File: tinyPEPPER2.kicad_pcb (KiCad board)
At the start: 2 copper layers, 20 x 22.6 mm, 91 parts, among them U201 EFM8BB10, U301 EFM8BB10, U401 EFM8BB10, U501 EFM8BB10

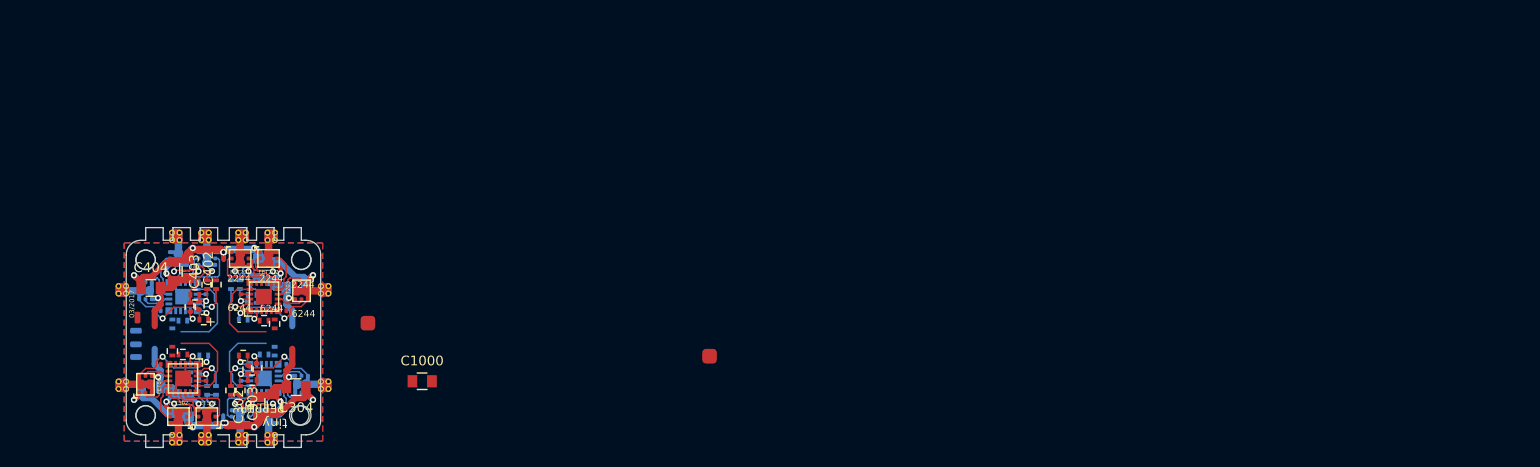
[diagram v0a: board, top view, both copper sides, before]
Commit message: adding gate druiver
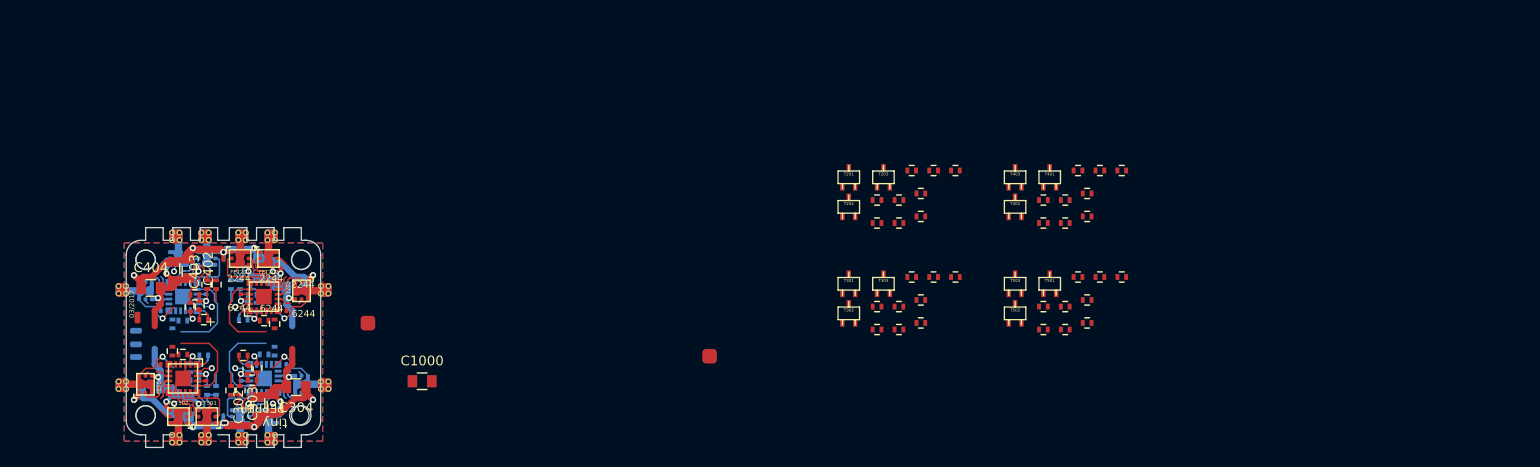
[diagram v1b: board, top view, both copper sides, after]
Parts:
- added R208: 2k2, custom:R_0402_CUSTOM, F.Cu at (180.8, 92.8)
- added R209: 2k2, custom:R_0402_CUSTOM, F.Cu at (177.2, 95.9)
- added R210: 2k2, custom:R_0402_CUSTOM, F.Cu at (181.7, 95.2)
- added R211: 1K, custom:R_0402_CUSTOM, F.Cu at (179.5, 98.2)
- added R212: 1K, custom:R_0402_CUSTOM, F.Cu at (185.3, 92.8)
- added R213: 1K, custom:R_0402_CUSTOM, F.Cu at (183.0, 92.8)
- added R217: 10k, custom:R_0402_CUSTOM, F.Cu at (181.7, 97.5)
- added R218: 10k, custom:R_0402_CUSTOM, F.Cu at (179.5, 95.9)
- added R219: 10k, custom:R_0402_CUSTOM, F.Cu at (177.2, 98.2)
- added R308: 2k2, custom:R_0402_CUSTOM, F.Cu at (181.7, 108.5)
- added R309: 2k2, custom:R_0402_CUSTOM, F.Cu at (185.3, 103.8)
- added R310: 2k2, custom:R_0402_CUSTOM, F.Cu at (179.5, 109.2)
- added R311: 1K, custom:R_0402_CUSTOM, F.Cu at (181.7, 106.1)
- added R312: 1K, custom:R_0402_CUSTOM, F.Cu at (183.0, 103.8)
- added R313: 1K, custom:R_0402_CUSTOM, F.Cu at (179.5, 106.8)
- added R317: 10k, custom:R_0402_CUSTOM, F.Cu at (177.2, 109.2)
- added R318: 10k, custom:R_0402_CUSTOM, F.Cu at (180.8, 103.8)
- added R319: 10k, custom:R_0402_CUSTOM, F.Cu at (177.2, 106.8)
- added R408: 2k2, custom:R_0402_CUSTOM, F.Cu at (197.9, 92.8)
- added R409: 2k2, custom:R_0402_CUSTOM, F.Cu at (194.3, 98.2)
- added R410: 2k2, custom:R_0402_CUSTOM, F.Cu at (196.6, 95.9)
- added R411: 1K, custom:R_0402_CUSTOM, F.Cu at (200.1, 92.8)
- added R412: 1K, custom:R_0402_CUSTOM, F.Cu at (198.8, 95.2)
- added R413: 1K, custom:R_0402_CUSTOM, F.Cu at (198.8, 97.5)
- added R417: 10k, custom:R_0402_CUSTOM, F.Cu at (194.3, 95.9)
- added R418: 10k, custom:R_0402_CUSTOM, F.Cu at (202.4, 92.8)
- added R419: 10k, custom:R_0402_CUSTOM, F.Cu at (196.6, 98.2)
- added R508: 2k2, custom:R_0402_CUSTOM, F.Cu at (197.9, 103.8)
- added R509: 2k2, custom:R_0402_CUSTOM, F.Cu at (194.3, 106.8)
- added R510: 2k2, custom:R_0402_CUSTOM, F.Cu at (198.8, 108.5)
- added R511: 1K, custom:R_0402_CUSTOM, F.Cu at (202.4, 103.8)
- added R512: 1K, custom:R_0402_CUSTOM, F.Cu at (196.6, 109.2)
- added R513: 1K, custom:R_0402_CUSTOM, F.Cu at (198.8, 106.1)
- added R517: 10k, custom:R_0402_CUSTOM, F.Cu at (200.1, 103.8)
- added R518: 10k, custom:R_0402_CUSTOM, F.Cu at (196.6, 106.8)
- added R519: 10k, custom:R_0402_CUSTOM, F.Cu at (194.3, 109.2)
- added T201: MMBTA06WT1G, custom:SC70, F.Cu at (174.3, 93.5)
- added T202: MMBTA06WT1G, custom:SC70, F.Cu at (174.3, 96.6)
- added T203: MMBTA06WT1G, custom:SC70, F.Cu at (177.9, 93.5)
- added T301: MMBTA06WT1G, custom:SC70, F.Cu at (174.3, 104.5)
- added T302: MMBTA06WT1G, custom:SC70, F.Cu at (174.3, 107.5)
- added T303: MMBTA06WT1G, custom:SC70, F.Cu at (177.9, 104.5)
- added T401: MMBTA06WT1G, custom:SC70, F.Cu at (195.0, 93.5)
- added T402: MMBTA06WT1G, custom:SC70, F.Cu at (191.4, 96.6)
- added T403: MMBTA06WT1G, custom:SC70, F.Cu at (191.4, 93.5)
- added T501: MMBTA06WT1G, custom:SC70, F.Cu at (195.0, 104.5)
- added T502: MMBTA06WT1G, custom:SC70, F.Cu at (191.4, 107.5)
- added T503: MMBTA06WT1G, custom:SC70, F.Cu at (191.4, 104.5)
- R202, R204, R206, R302, R304, R306, R402, R404, R406, R502, R504, R506: value 1k -> 10k
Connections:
- FET201 pad 5: /single esc 1/Ac_0 -> Net-(FET201-Pad5)
- FET202 pad 5: /single esc 1/Bc_0 -> Net-(FET202-Pad5)
- FET203 pad 5: /single esc 1/Cc_0 -> Net-(FET203-Pad5)
- FET301 pad 5: /single esc 2/Ac_0 -> Net-(FET301-Pad5)
- FET302 pad 5: /single esc 2/Bc_0 -> Net-(FET302-Pad5)
- FET303 pad 5: /single esc 2/Cc_0 -> Net-(FET303-Pad5)
- FET401 pad 5: /single esc 3/Ac_0 -> Net-(FET401-Pad5)
- FET402 pad 5: /single esc 3/Bc_0 -> Net-(FET402-Pad5)
- FET403 pad 5: /single esc 3/Cc_0 -> Net-(FET403-Pad5)
- FET501 pad 5: /single esc 4/Ac_0 -> Net-(FET501-Pad5)
- FET502 pad 5: /single esc 4/Bc_0 -> Net-(FET502-Pad5)
- FET503 pad 5: /single esc 4/Cc_0 -> Net-(FET503-Pad5)
- R201 pad 1: Net-(R201-Pad1) -> VCC
- R201 pad 2: VCC -> /single esc 1/C2CK_0
- R202 pad 2: /single esc 1/PHASE_A_0 -> Net-(R202-Pad2)
- R203 pad 1: /single esc 1/PHASE_A_0 -> Net-(R202-Pad2)
- R203 pad 2: Net-(R203-Pad2) -> /single esc 1/PHASE_A_0
- R204 pad 2: /single esc 1/PHASE_B_0 -> Net-(R204-Pad2)
- R205 pad 1: /single esc 1/PHASE_B_0 -> Net-(R204-Pad2)
- R205 pad 2: Net-(R205-Pad2) -> /single esc 1/PHASE_B_0
- R206 pad 2: /single esc 1/PHASE_C_0 -> Net-(R206-Pad2)
- R207 pad 1: /single esc 1/PHASE_C_0 -> Net-(R206-Pad2)
- R207 pad 2: Net-(R207-Pad2) -> /single esc 1/PHASE_C_0
- R301 pad 1: Net-(R301-Pad1) -> VCC
- R301 pad 2: VCC -> /single esc 2/C2CK_0
- R302 pad 2: /single esc 2/PHASE_A_0 -> Net-(R302-Pad2)
- R303 pad 1: /single esc 2/PHASE_A_0 -> Net-(R302-Pad2)
- R303 pad 2: Net-(R303-Pad2) -> /single esc 2/PHASE_A_0
- R304 pad 2: /single esc 2/PHASE_B_0 -> Net-(R304-Pad2)
- R305 pad 1: /single esc 2/PHASE_B_0 -> Net-(R304-Pad2)
- R305 pad 2: Net-(R305-Pad2) -> /single esc 2/PHASE_B_0
- R306 pad 2: /single esc 2/PHASE_C_0 -> Net-(R306-Pad2)
- R307 pad 1: /single esc 2/PHASE_C_0 -> Net-(R306-Pad2)
- R307 pad 2: Net-(R307-Pad2) -> /single esc 2/PHASE_C_0
- R401 pad 1: Net-(R401-Pad1) -> VCC
- R401 pad 2: VCC -> /single esc 3/C2CK_0
- R402 pad 2: /single esc 3/PHASE_A_0 -> Net-(R402-Pad2)
- R403 pad 1: /single esc 3/PHASE_A_0 -> Net-(R402-Pad2)
- R403 pad 2: Net-(R403-Pad2) -> /single esc 3/PHASE_A_0
- R404 pad 2: /single esc 3/PHASE_B_0 -> Net-(R404-Pad2)
- R405 pad 1: /single esc 3/PHASE_B_0 -> Net-(R404-Pad2)
- R405 pad 2: Net-(R405-Pad2) -> /single esc 3/PHASE_B_0
- R406 pad 2: /single esc 3/PHASE_C_0 -> Net-(R406-Pad2)
- R407 pad 1: /single esc 3/PHASE_C_0 -> Net-(R406-Pad2)
- R407 pad 2: Net-(R407-Pad2) -> /single esc 3/PHASE_C_0
- R501 pad 1: Net-(R501-Pad1) -> VCC
- R501 pad 2: VCC -> /single esc 4/C2CK_0
- R502 pad 2: /single esc 4/PHASE_A_0 -> Net-(R502-Pad2)
- R503 pad 1: /single esc 4/PHASE_A_0 -> Net-(R502-Pad2)
- R503 pad 2: Net-(R503-Pad2) -> /single esc 4/PHASE_A_0
- R504 pad 2: /single esc 4/PHASE_B_0 -> Net-(R504-Pad2)
- R505 pad 1: /single esc 4/PHASE_B_0 -> Net-(R504-Pad2)
- R505 pad 2: Net-(R505-Pad2) -> /single esc 4/PHASE_B_0
- R506 pad 2: /single esc 4/PHASE_C_0 -> Net-(R506-Pad2)
- R507 pad 1: /single esc 4/PHASE_C_0 -> Net-(R506-Pad2)
- R507 pad 2: Net-(R507-Pad2) -> /single esc 4/PHASE_C_0
- U201 pad 1: Net-(R207-Pad2) -> Net-(R206-Pad2)
- U201 pad 2: Net-(R205-Pad2) -> Net-(R204-Pad2)
- U201 pad 20: Net-(R203-Pad2) -> Net-(R202-Pad2)
- U201 pad 5: Net-(R201-Pad1) -> /single esc 1/C2CK_0
- U201 pad 8: /single esc 1/Cc_0 -> Net-(R213-Pad2)
- U301 pad 1: Net-(R307-Pad2) -> Net-(R306-Pad2)
- U301 pad 2: Net-(R305-Pad2) -> Net-(R304-Pad2)
- U301 pad 20: Net-(R303-Pad2) -> Net-(R302-Pad2)
- U301 pad 5: Net-(R301-Pad1) -> /single esc 2/C2CK_0
- U301 pad 8: /single esc 2/Cc_0 -> Net-(R313-Pad2)
- U401 pad 1: Net-(R407-Pad2) -> Net-(R406-Pad2)
- U401 pad 2: Net-(R405-Pad2) -> Net-(R404-Pad2)
- U401 pad 20: Net-(R403-Pad2) -> Net-(R402-Pad2)
- U401 pad 5: Net-(R401-Pad1) -> /single esc 3/C2CK_0
- U401 pad 8: /single esc 3/Cc_0 -> Net-(R413-Pad2)
- U501 pad 1: Net-(R507-Pad2) -> Net-(R506-Pad2)
- U501 pad 2: Net-(R505-Pad2) -> Net-(R504-Pad2)
- U501 pad 20: Net-(R503-Pad2) -> Net-(R502-Pad2)
- U501 pad 5: Net-(R501-Pad1) -> /single esc 4/C2CK_0
- U501 pad 8: /single esc 4/Cc_0 -> Net-(R513-Pad2)
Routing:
- net /single esc 3/PHASE_B_0: track 13.9 -> 6.85 mm
- net /single esc 1/PHASE_B_0: track 13.9 -> 6.85 mm
- net /single esc 4/PHASE_B_0: track 13.9 -> 6.85 mm
- net /single esc 2/PHASE_B_0: track 13.9 -> 6.85 mm
- net Net-(R404-Pad2): track 0.00 -> 6.74 mm, vias 0 -> 1
- net Net-(R204-Pad2): track 0.00 -> 6.74 mm, vias 0 -> 1
- net Net-(R504-Pad2): track 0.00 -> 6.74 mm, vias 0 -> 1
- net Net-(R304-Pad2): track 0.00 -> 6.74 mm, vias 0 -> 1
- net Net-(R302-Pad2): track 0.00 -> 4.07 mm, vias 0 -> 1
- net Net-(R402-Pad2): track 0.00 -> 4.07 mm, vias 0 -> 1
- net Net-(R502-Pad2): track 0.00 -> 3.78 mm, vias 0 -> 1
- net Net-(R202-Pad2): track 0.00 -> 3.78 mm, vias 0 -> 1
- net Net-(R503-Pad2): track 3.65 -> 0.00 mm, vias 1 -> 0
- net Net-(R303-Pad2): track 3.65 -> 0.00 mm, vias 1 -> 0
- net Net-(R403-Pad2): track 3.65 -> 0.00 mm, vias 1 -> 0
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
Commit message: routing test done
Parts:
- added C1001: 100n, custom:C_0402_CUSTOM, F.Cu at (89.7, 109.5)
- added C1002: 100n, custom:C_0402_CUSTOM, F.Cu at (89.7, 111.9)
- added C1003: 10n, custom:C_0402_CUSTOM, F.Cu at (105.3, 110.1)
- added R214: 100, custom:R_0603_CUSTOM, F.Cu at (215.6, 94.8)
- added R215: 100, custom:R_0603_CUSTOM, F.Cu at (220.0, 94.8)
- added R216: 100, custom:R_0603_CUSTOM, F.Cu at (224.3, 94.8)
- added R314: 100, custom:R_0603_CUSTOM, F.Cu at (215.6, 105.6)
- added R315: 100, custom:R_0603_CUSTOM, F.Cu at (220.0, 105.6)
- added R316: 100, custom:R_0603_CUSTOM, F.Cu at (224.3, 105.6)
- added R414: 100, custom:R_0603_CUSTOM, F.Cu at (232.5, 94.8)
- added R415: 100, custom:R_0603_CUSTOM, F.Cu at (236.8, 94.8)
- added R416: 100, custom:R_0603_CUSTOM, F.Cu at (241.1, 94.8)
- added R514: 100, custom:R_0603_CUSTOM, B.Cu at (109.4, 116.5)
- added R515: 100, custom:R_0603_CUSTOM, B.Cu at (105.6, 116.2)
- added R516: 100, custom:R_0603_CUSTOM, F.Cu at (102.1, 112.9)
- added U1: AP131-30, TO_SOT_Packages_SMD:SOT-23-5, F.Cu at (102.6, 110.0)
- R508, R509, R510, R511, R513, R517, R518, R519: moved to B.Cu
- T201, T202, T203, T301, T302, T303, T401, T402, T403: value MMBTA06WT1G -> BC847BTT1G; footprint custom:SC70 -> custom:SC75
- T501, T502, T503: value MMBTA06WT1G -> BC847BTT1G; footprint custom:SC70 -> custom:SC75; moved to B.Cu
- TP104, TP106: moved to F.Cu
- moved R513 95.9 mm to (103.1, 112.8)
- moved R511 95.8 mm to (107.5, 117.3), turned to 90 degrees
- moved R517 93.7 mm to (107.7, 118.8), turned to 90 degrees
- moved R519 92.9 mm to (101.5, 113.3)
- moved R510 92.8 mm to (106.2, 112.8), turned to 180 degrees
- moved R512 92.4 mm to (104.5, 116.8), turned to 180 degrees
- moved R518 91.2 mm to (105.9, 117.1), turned to 180 degrees
- moved R508 90.7 mm to (107.7, 112.8)
- moved T503 90.5 mm to (101.5, 114.9), turned to 270 degrees
- moved R509 88.3 mm to (106.3, 113.8), turned to 180 degrees
- moved T501 87.0 mm to (109.1, 118.6)
- moved T502 86.9 mm to (105.2, 118.6)
- moved C201 65.8 mm to (176.3, 86.7)
- moved C203 65.8 mm to (177.3, 81.6)
- moved OUT_A401 65.8 mm to (170.2, 78.0)
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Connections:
- C201 pad 2: VCC -> /single esc 1/3V3
- C301 pad 2: VCC -> /single esc 1/3V3
- C401 pad 2: VCC -> /single esc 1/3V3
- C501 pad 2: VCC -> /single esc 1/3V3
- R201 pad 1: VCC -> /single esc 1/3V3
- R301 pad 1: VCC -> /single esc 1/3V3
- R401 pad 1: VCC -> /single esc 1/3V3
- R501 pad 1: VCC -> /single esc 1/3V3
- T201 pad 3: (no net) -> GND
- T202 pad 3: (no net) -> GND
- T203 pad 3: (no net) -> GND
- T301 pad 3: (no net) -> GND
- T302 pad 3: (no net) -> GND
- T303 pad 3: (no net) -> GND
- T401 pad 3: (no net) -> GND
- T402 pad 3: (no net) -> GND
- T403 pad 3: (no net) -> GND
- T501 pad 3: (no net) -> GND
- T502 pad 3: (no net) -> GND
- T503 pad 3: (no net) -> GND
- U201 pad 4: VCC -> /single esc 1/3V3
- U301 pad 4: VCC -> /single esc 1/3V3
- U401 pad 4: VCC -> /single esc 1/3V3
- U501 pad 4: VCC -> /single esc 1/3V3
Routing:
- net GND: track 85.5 -> 44.5 mm, vias 12 -> 5
- net VCC: track 59.6 -> 33.9 mm, vias 12 -> 4
- net (no net): track 0.00 -> 17.7 mm
- net /single esc 3/PHASE_C_0: track 10.9 -> 0.00 mm, vias 1 -> 0
- net /single esc 1/PHASE_C_0: track 10.9 -> 0.00 mm, vias 1 -> 0
- net /single esc 2/PHASE_C_0: track 10.9 -> 0.00 mm, vias 1 -> 0
- net /single esc 3/RC_IN: track 9.27 -> 0.00 mm
- net /RC_IN_0: track 9.27 -> 0.00 mm
- net /RC_IN_1: track 9.27 -> 0.00 mm
- net /single esc 2/PHASE_A_0: track 7.72 -> 0.00 mm
- net /single esc 1/PHASE_A_0: track 7.72 -> 0.00 mm
- net /single esc 3/PHASE_A_0: track 7.72 -> 0.00 mm
- net /single esc 2/PHASE_B_0: track 6.85 -> 0.00 mm, vias 1 -> 0
- net /single esc 3/PHASE_B_0: track 6.85 -> 0.00 mm, vias 1 -> 0
- net /single esc 1/PHASE_B_0: track 6.85 -> 0.00 mm, vias 1 -> 0
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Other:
- board text removed: "REV 0.4"

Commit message: 4in1
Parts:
- C1000, C1002, C402, C403, C404, R208, R209, R210, R211, R213, R214, R215, R217, R218, R219, R312, R316, R412, R416, T201, T202, T203, TP101, TP102: moved to B.Cu
- R301, R401, TP103: moved to F.Cu
- moved R416 124.5 mm to (117.9, 112.9)
- moved R415 124.3 mm to (114.4, 116.2)
- moved R414 123.8 mm to (110.6, 116.5), turned to 270 degrees
- moved R316 122.2 mm to (102.1, 107.1), turned to 180 degrees
- moved R315 114.3 mm to (105.6, 103.8), turned to 180 degrees
- moved R216 107.0 mm to (117.9, 107.1)
- moved R314 106.3 mm to (109.4, 103.4), turned to 90 degrees
- moved R215 105.9 mm to (114.4, 103.7)
- moved R214 105.4 mm to (110.6, 103.4), turned to 90 degrees
- moved R418 91.5 mm to (114.1, 117.2)
- moved R411 91.0 mm to (112.5, 117.3), turned to 90 degrees
- moved R408 87.8 mm to (112.4, 112.8), turned to 180 degrees
- moved T401 87.7 mm to (110.9, 118.6), turned to 180 degrees
- moved R412 86.0 mm to (115.5, 116.8)
- moved R417 85.1 mm to (112.4, 118.8), turned to 90 degrees
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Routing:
- net GND: track 44.5 -> 213.7 mm, vias 5 -> 25
- net VCC: track 33.9 -> 110.0 mm, vias 4 -> 17
- net /single esc 1/3V3: track 2.93 -> 32.6 mm, vias 0 -> 2
- net (no net): track 17.7 -> 0.00 mm
- net /single esc 3/PHASE_B_0: track 0.00 -> 12.0 mm, vias 0 -> 1
- net /single esc 1/PHASE_B_0: track 0.00 -> 12.0 mm, vias 0 -> 1
- net /single esc 2/PHASE_B_0: track 0.00 -> 12.0 mm, vias 0 -> 1
- net /single esc 3/PHASE_C_0: track 0.00 -> 12.0 mm, vias 0 -> 1
- net /single esc 1/PHASE_C_0: track 0.00 -> 12.0 mm, vias 0 -> 1
- net /single esc 2/PHASE_C_0: track 0.00 -> 11.8 mm, vias 0 -> 1
- net Net-(R306-Pad2): track 0.00 -> 9.34 mm, vias 0 -> 1
- net Net-(R406-Pad2): track 0.00 -> 9.34 mm, vias 0 -> 1
- net Net-(R206-Pad2): track 0.00 -> 9.34 mm, vias 0 -> 1
- net /single esc 3/Ap_0: track 0.00 -> 8.37 mm
- net /single esc 2/Ap_0: track 0.00 -> 8.37 mm
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
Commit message: caps
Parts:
- C1000, C202, C203, C204, C402, C403, C404, C502, C503, C504: footprint custom:C_0805_CUSTOM -> custom:C_0603_CUSTOM
- C302, C303, C304: footprint custom:C_0805_CUSTOM -> custom:C_0603_CUSTOM; moved to B.Cu
- moved C204 29.1 mm to (102.5, 110.0), turned to 270 degrees
- moved C404 26.1 mm to (103.5, 110.0), turned to 270 degrees
- moved C304 22.1 mm to (104.6, 110.0), turned to 270 degrees
- moved C303 20.0 mm to (107.7, 110.0)
- moved C202 19.5 mm to (112.3, 110.0), turned to 270 degrees
- moved C203 17.0 mm to (115.4, 110.0), turned to 270 degrees
- moved C403 16.2 mm to (113.3, 110.0), turned to 270 degrees
- moved C402 15.1 mm to (114.4, 110.0), turned to 270 degrees
- moved C302 8.37 mm to (118.6, 110.0)
- moved C502 2.40 mm to (105.6, 110.0), turned to 270 degrees
- moved C503 0.70 mm to (117.5, 110.0)
- moved C504 0.15 mm to (106.7, 110.0), turned to 270 degrees

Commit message: first routing ok
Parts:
- OUT_A201, OUT_A301, OUT_A401, OUT_A501, OUT_B201, OUT_B301, OUT_B401, OUT_B501, OUT_C201, OUT_C301, OUT_C401, OUT_C501: footprint custom:TP_PHASE_SMD -> custom:TP_PHASE_PAD
- T201, T202, T203, T301, T302, T303, T401, T402, T403, T501, T502, T503: value BC847BTT1G -> BC847
- moved TP102 8.80 mm to (118.8, 108.8)
- moved TP101 8.75 mm to (118.8, 111.0)
- moved C302 8.55 mm to (110.0, 110.0)
- moved C503 6.25 mm to (111.3, 110.0)
- moved C403 4.20 mm to (117.5, 110.0)
- moved R401 1.38 mm to (115.6, 110.9), turned to 0 degrees
- moved C1001 1.25 mm to (106.4, 110.2), turned to 0 degrees
- moved C303 1.05 mm to (108.8, 110.0)
- moved C504 0.85 mm to (107.5, 110.0)
- moved C502 0.65 mm to (106.3, 110.0)
- moved C402 0.60 mm to (113.8, 110.0)
- moved OUT_A201 0.49 mm to (112.0, 100.0), turned to 0 degrees
- moved OUT_B201 0.49 mm to (115.0, 100.0), turned to 0 degrees
- moved OUT_A301 0.47 mm to (108.0, 100.0), turned to 180 degrees
- moved OUT_B301 0.47 mm to (105.0, 100.0), turned to 180 degrees
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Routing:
- net GND: track 213.7 -> 228.0 mm, vias 25 -> 29
- net VCC: track 109.8 -> 122.0 mm
- net Net-(R304-Pad2): track 5.70 -> 7.93 mm
- net Net-(R306-Pad2): track 9.34 -> 11.1 mm
- net Net-(R406-Pad2): track 9.34 -> 10.6 mm
- net Net-(R404-Pad2): track 5.70 -> 6.89 mm
- net /single esc 1/3V3: track 32.6 -> 33.5 mm
- net /single esc 3/C2CK_0: track 3.26 -> 2.68 mm
- net /single esc 1/PHASE_B_0: track 12.0 -> 11.5 mm
- net /single esc 2/PHASE_B_0: track 12.0 -> 11.5 mm
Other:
- board size 20 x 22.6 mm -> 20 x 20 mm
- board text added: "(c) fishpepper"
- board text added: "rev 0.1 02/17"
- board text removed: "03/2017"
- board text removed: "2244"
- board text removed: "6244"
- board text removed: "PEPPER"
- board text removed: "tiny"

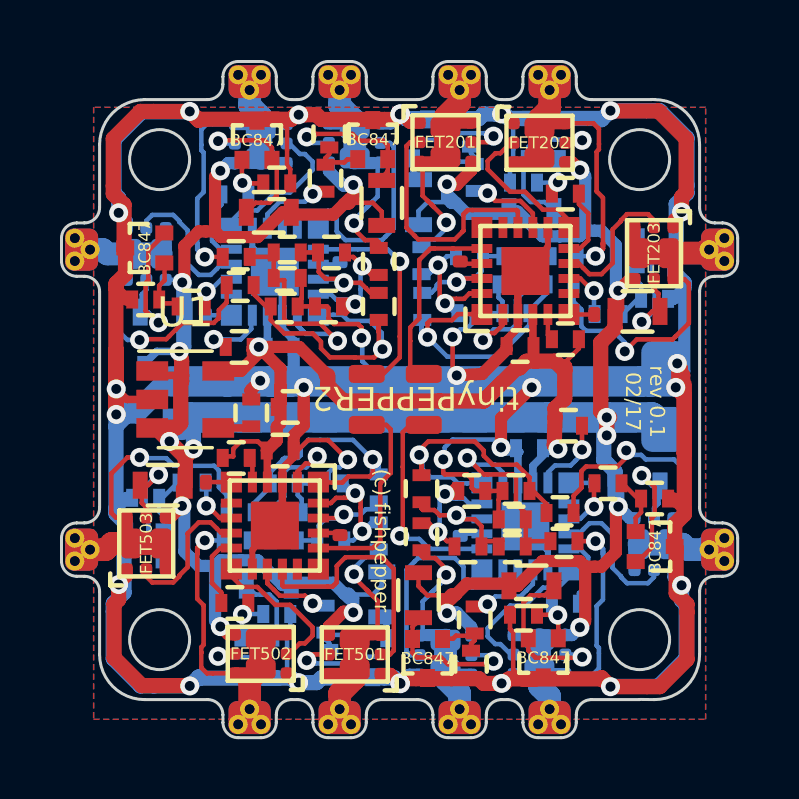
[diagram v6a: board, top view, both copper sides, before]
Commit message: added serial R
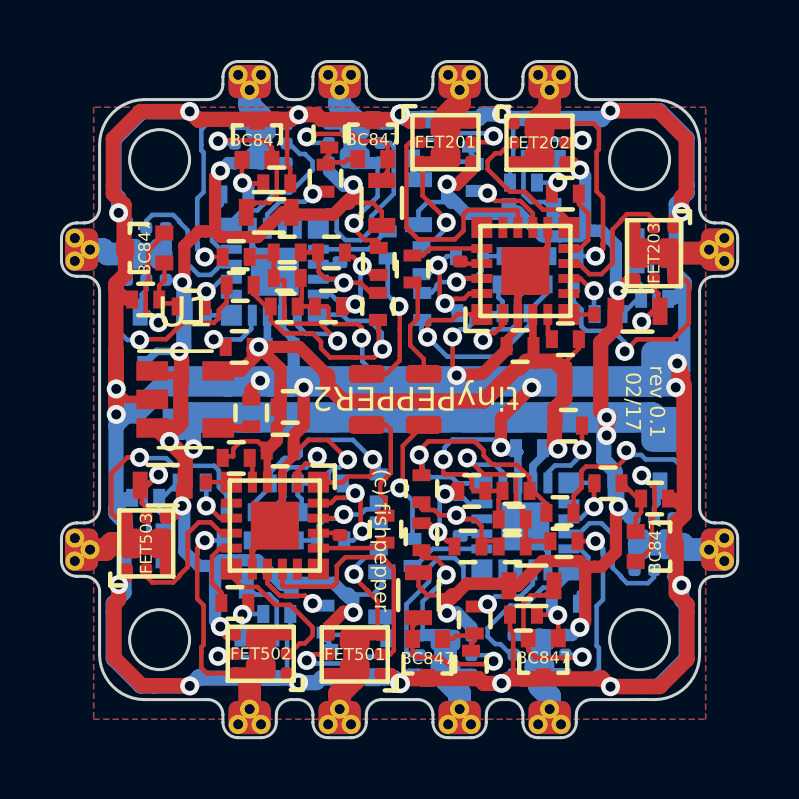
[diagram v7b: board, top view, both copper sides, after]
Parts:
- added R220: 1k, custom:R_0402_CUSTOM, F.Cu at (110.4, 105.6)
- added R320: 1k, custom:R_0402_CUSTOM, B.Cu at (109.6, 104.8)
- added R420: 1k, custom:R_0402_CUSTOM, B.Cu at (110.4, 115.1)
- added R520: 1k, custom:R_0402_CUSTOM, F.Cu at (109.5, 114.3)
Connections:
- U201 pad 17: /RC_IN_0 -> Net-(R220-Pad2)
- U301 pad 17: /RC_IN_1 -> Net-(R320-Pad2)
- U401 pad 17: /single esc 3/RC_IN -> Net-(R420-Pad2)
- U501 pad 17: /single esc 4/RC_IN -> Net-(R520-Pad2)
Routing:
- net /single esc 4/RC_IN: track 6.93 -> 4.00 mm
- net /RC_IN_0: track 6.88 -> 4.27 mm
- net Net-(R320-Pad2): track 0.00 -> 2.56 mm
- net Net-(R420-Pad2): track 0.00 -> 2.55 mm
- net /single esc 3/RC_IN: track 7.61 -> 5.16 mm
- net Net-(R220-Pad2): track 0.00 -> 2.41 mm
- net /RC_IN_1: track 7.99 -> 5.65 mm
- net Net-(R520-Pad2): track 0.00 -> 2.31 mm

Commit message: 4layer done
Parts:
- removed TP101, TP102: TP, custom:TP_powerpad
- added TP10: TP, custom:TP_powerpad, B.Cu at (119.0, 110.8)
- added TP11: TP, custom:TP_powerpad, F.Cu at (119.0, 110.8)
- added TP12: TP, custom:TP_powerpad, B.Cu at (119.0, 108.9)
- added TP13: TP, custom:TP_powerpad, F.Cu at (119.0, 108.9)
- added TP203: TP, custom:TP_smd_0.5x0.4, F.Cu at (115.7, 108.0)
- added TP303: TP, custom:TP_smd_0.5x0.4, B.Cu at (104.5, 108.1)
- added TP403: TP, custom:TP_smd_0.5x0.4, B.Cu at (116.1, 112.0)
- added TP503: TP, custom:TP_smd_0.5x0.4, F.Cu at (103.7, 112.1)
- moved R201 1.29 mm to (115.9, 109.2), turned to 90 degrees
- moved R301 0.38 mm to (104.7, 107.9)
- moved R501 0.34 mm to (104.6, 111.6), turned to 180 degrees
- moved R413 0.24 mm to (116.7, 112.8)
- moved U1 0.16 mm to (102.9, 109.8)
- moved TP402 0.13 mm to (116.4, 112.9), turned to 180 degrees
- moved R416 0.08 mm to (117.9, 113.0)
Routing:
- net VCC: track 122.0 -> 127.4 mm, vias 17 -> 23
- net /single esc 1/3V3: track 33.5 -> 31.0 mm
- net GND: track 228.0 -> 230.4 mm, vias 29 -> 31
- net /single esc 4/C2CK_0: track 0.88 -> 2.47 mm
- net /single esc 1/C2CK_0: track 0.88 -> 2.34 mm
- net /single esc 3/PHASE_C_0: track 12.1 -> 11.4 mm
- net /single esc 2/C2CK_0: track 2.37 -> 3.08 mm
- added copper zone on In1.Cu, net GND
- added copper zone on In2.Cu, net VCC
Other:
- copper layers 2 -> 4
- board text added: "rev 0.2 02/17"
- board text removed: "rev 0.1 02/17"
